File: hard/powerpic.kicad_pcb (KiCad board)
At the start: 2 copper layers, 25.6 x 27.6 mm, 21 parts, among them U1 PIC16LF1919x-I/MR

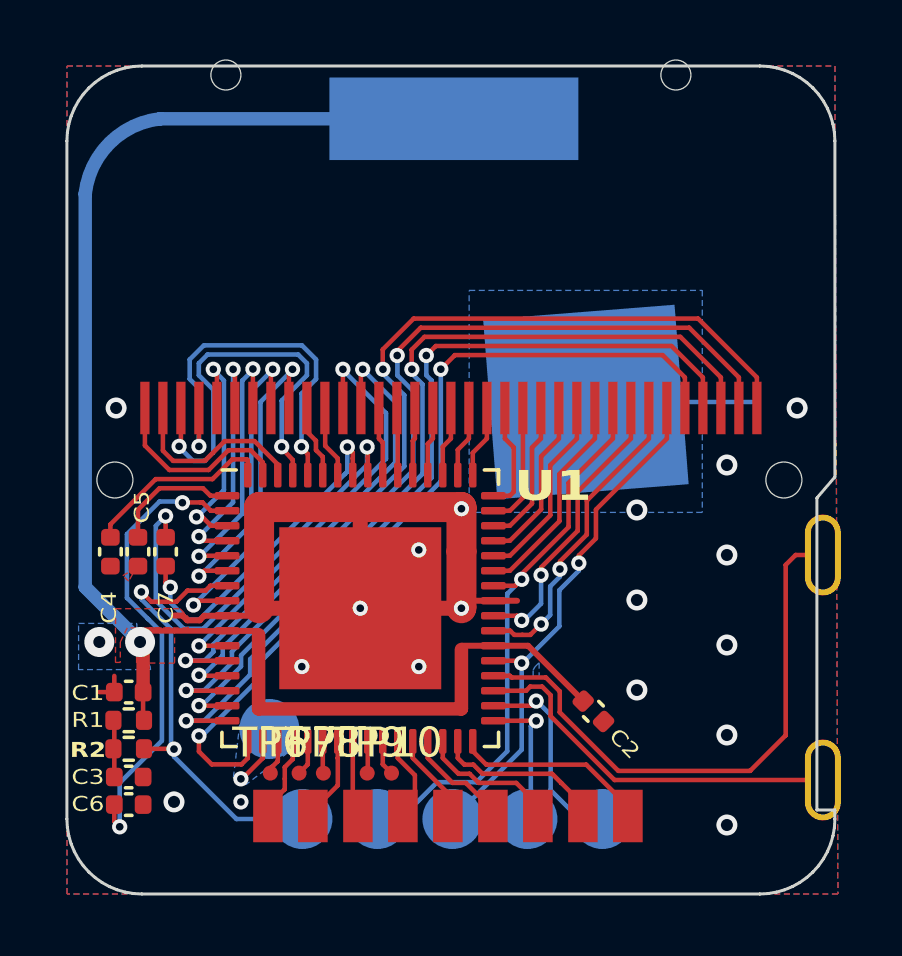
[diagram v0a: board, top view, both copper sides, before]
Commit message: Added some silkscreen labels, and noticed a design error. Final commit before version bump
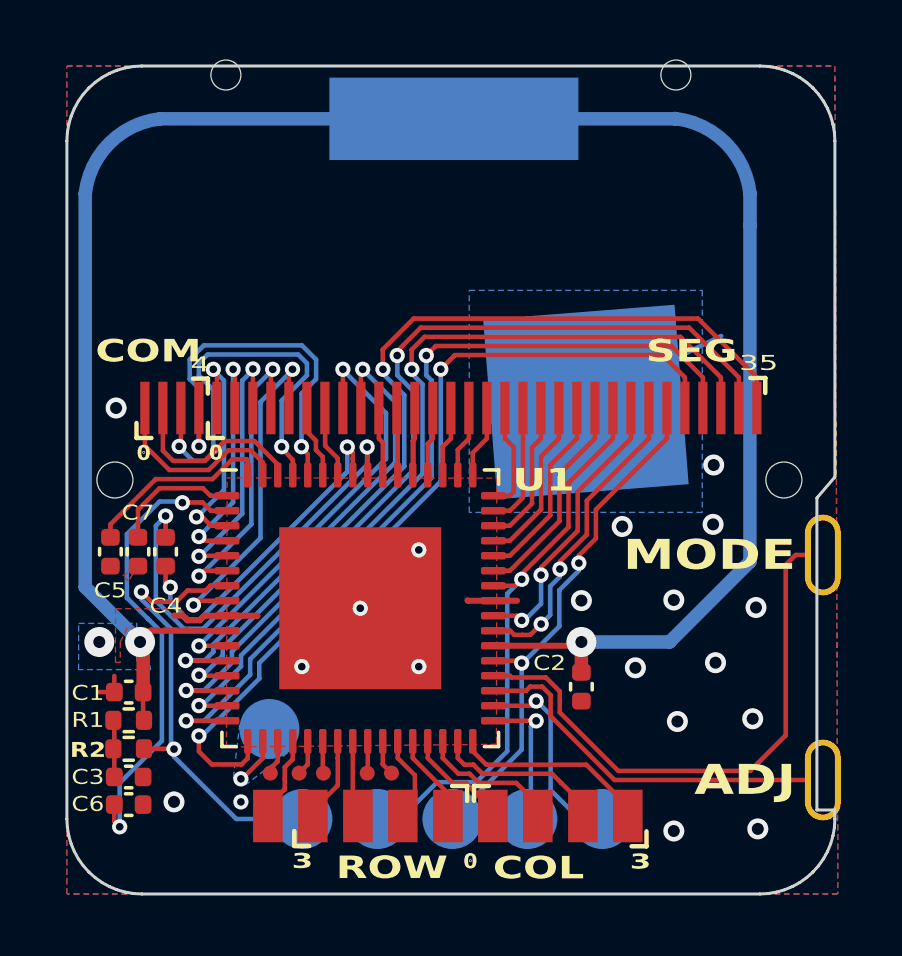
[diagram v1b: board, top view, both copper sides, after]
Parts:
- moved C2 0.91 mm to (144.2, 69.3), turned to 90 degrees
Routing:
- net GND: track 35.8 -> 10.7 mm, vias 19 -> 20
- net VCC: track 52.3 -> 69.4 mm, vias 1 -> 2
- removed copper zone on F.Cu, net VCC
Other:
- board text added: "0"
- board text added: "3"
- board text added: "35"
- board text added: "4"
- board text added: "ADJ"
- board text added: "COL"
- board text added: "COM"
- board text added: "MODE"
- board text added: "ROW"
- board text added: "SEG"

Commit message: Version 1.0 of pcb
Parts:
- moved C7 8.45 mm to (129.1, 73.2), turned to 0 degrees
- moved C6 8.44 mm to (129.4, 64.8), turned to -90 degrees
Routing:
- net /VLCD1: track 15.6 -> 3.87 mm, vias 2 -> 0
- net /VLCD2: track 4.29 -> 15.6 mm, vias 0 -> 2
- net /SEG0: track 7.94 -> 8.65 mm
- net GND: vias 20 -> 15
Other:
- board text added: "Designed in Oakland CA by Rex McKinnon Feb '22"
- board text added: "PIC"
- board text added: "Power"
- board text added: "v1.0"

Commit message: Version 1.1 Release
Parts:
- removed TP10: RH0, powerpic:TestPoint_Pad_D0.5mm
- removed TP6: RG7, powerpic:TestPoint_Pad_D0.5mm
- removed TP7: RA3, powerpic:TestPoint_Pad_D0.5mm
- removed TP8: RA2, powerpic:TestPoint_Pad_D0.5mm
- removed TP9: RH1, powerpic:TestPoint_Pad_D0.5mm
- added GND: Progo_Pad_D2.0mm, powerpic:Progo_Pad_D2.0mm, B.Cu at (147.3, 73.7)
- turned TP5 to -90 degrees
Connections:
- U1 pad 18: /BUZZ -> unconnected-(U1-SEG41/RF0)
- U1 pad 19: /RG7 -> /BUZZ
- U1 pad 21: /RA3 -> /ROW3
- U1 pad 22: /RA2 -> /ROW2
- U1 pad 23: /ROW3 -> /ROW1
- U1 pad 24: /ROW2 -> /ROW0
- U1 pad 27: /ROW1 -> unconnected-(U1-RA5)
- U1 pad 28: /ROW0 -> unconnected-(U1-RA4/SEG14)
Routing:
- net GND: track 10.7 -> 15.7 mm, vias 15 -> 20
- net /ROW0: track 2.97 -> 5.51 mm
- net /ROW1: track 2.89 -> 4.53 mm
- net /RH0: track 1.18 -> 0.00 mm
- net /RA3: track 1.18 -> 0.00 mm
- net /RG7: track 1.16 -> 0.00 mm
- net /RH1: track 1.07 -> 0.00 mm
- net /RA2: track 1.05 -> 0.00 mm
- net /ROW2: track 2.56 -> 3.21 mm
- net /BUZZ: track 1.57 -> 0.94 mm
- net /MODE: track 19.0 -> 18.4 mm
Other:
- board text added: "30"
- board text added: "BUZ"
- board text added: "Designed in Oakland CA by Rex McKinnon March '22"
- board text added: "v1.1"
- board text removed: "35"
- board text removed: "Designed in Oakland CA by Rex McKinnon Feb '22"
- board text removed: "v1.0"
